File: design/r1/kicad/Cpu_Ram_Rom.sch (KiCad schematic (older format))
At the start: 14 parts, among them IC1 MC68010P10, U1 AT28C64B-15PU, U2 AT28C64B-15PU, U3 AS6C4008-55PCN, U4 AS6C4008-55PCN

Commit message: Initial cleanup
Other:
- note added: "1"
- note added: "CPU, RAM & ROM"
- note added: "Copyright ©2019-2020 Ross Bamford and Contributors.\nOpen Source Hardware licenced under CERN Open Hardware Licence. \nSee https://github.com/roscopeco/rosco_m68k/blob/master/LICENCE.hardware.txt\nOSHWA UK000006 (https://certification.oshwa.org/uk000006.html)\n"
- note removed: "CPU, RAM\n& ROM"
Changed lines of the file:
@@
-$EndComp
-$Comp
-L rosco_m68k-eagle-import:A3L-LOC #FRAME1
-U 1 1 CBB98AC2
-P 900 10700
-AR Path="/CBB98AC2" Ref="#FRAME1"  Part="1"
-AR Path="/5E53B4B8/CBB98AC2" Ref="#FRAME1"  Part="1"
-F 0 "#FRAME1" H 900 10700 50  0001 C CNN
-F 1 "CPU" H 900 10700 50  0001 C CNN
-F 2 "" H 900 10700 50  0001 C CNN
-F 3 "" H 900 10700 50  0001 C CNN
-	1    900  10700
-	1    0    0    -1
 $EndComp
 $Comp
@@
 Text Notes 14100 8900 0    59   ~ 0
 EVEN
-Text Notes 12700 10400 0    170  ~ 0
-CPU, RAM\n& ROM
 NoConn ~ 4400 2400
 NoConn ~ 4400 2500
@@
 Wire Bus Line
 	7500 550  7500 2600
+Connection ~ 7500 550
+Wire Bus Line
+	7500 550  2500 550
+Text Notes 19800 10900 0    50   ~ 0
+1
+Text Notes 16550 10750 0    79   ~ 0
+CPU, RAM & ROM
+Text Notes 16200 10200 0    59   ~ 0
+Copyright ©2019-2020 Ross Bamford and Contributors.\nOpen Source Hardware licenced under CERN Open Hardware Licence. \nSee https://github.com/roscopeco/rosco_m68k/blob/master/LICENCE.hardware.txt\nOSHWA UK000006 (https://certification.oshwa.org/uk000006.html)\n
 Wire Bus Line
 	11900 5300 11900 6100
@@
 Wire Bus Line
 	11450 2900 11450 4800
-Connection ~ 7500 550
-Wire Bus Line
-	7500 550  2500 550
 $EndSCHEMATC

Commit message: Cleanup first pass
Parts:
- U3, U4: symbol rosco_m68k-eagle-import:AS6C4008-55PCN -> rosco_m68k-rescue:AS6C4008-55PCN-rosco_m68k-eagle-import
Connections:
- net labels added: HALT, RAMOE, RW
- net labels removed: /HALT, /RAMOE, CONTROL:AS,BERR,BG,BGACK,BR,CLK,DTACK,EVENRAMSEL,EVENROMSEL,EXPSEL,FC0,FC1,FC2,IOSEL,IPL0,IPL1,IPL2,LDS,ODDRAMSEL,ODDROMSEL,RESET,R/W,UDS, R/W
- wire segments 240 -> 219
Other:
- moved on the sheet: C1, C2, C3, C4, C5, C6, C7, C8, IC1A, IC1B, R1, U1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

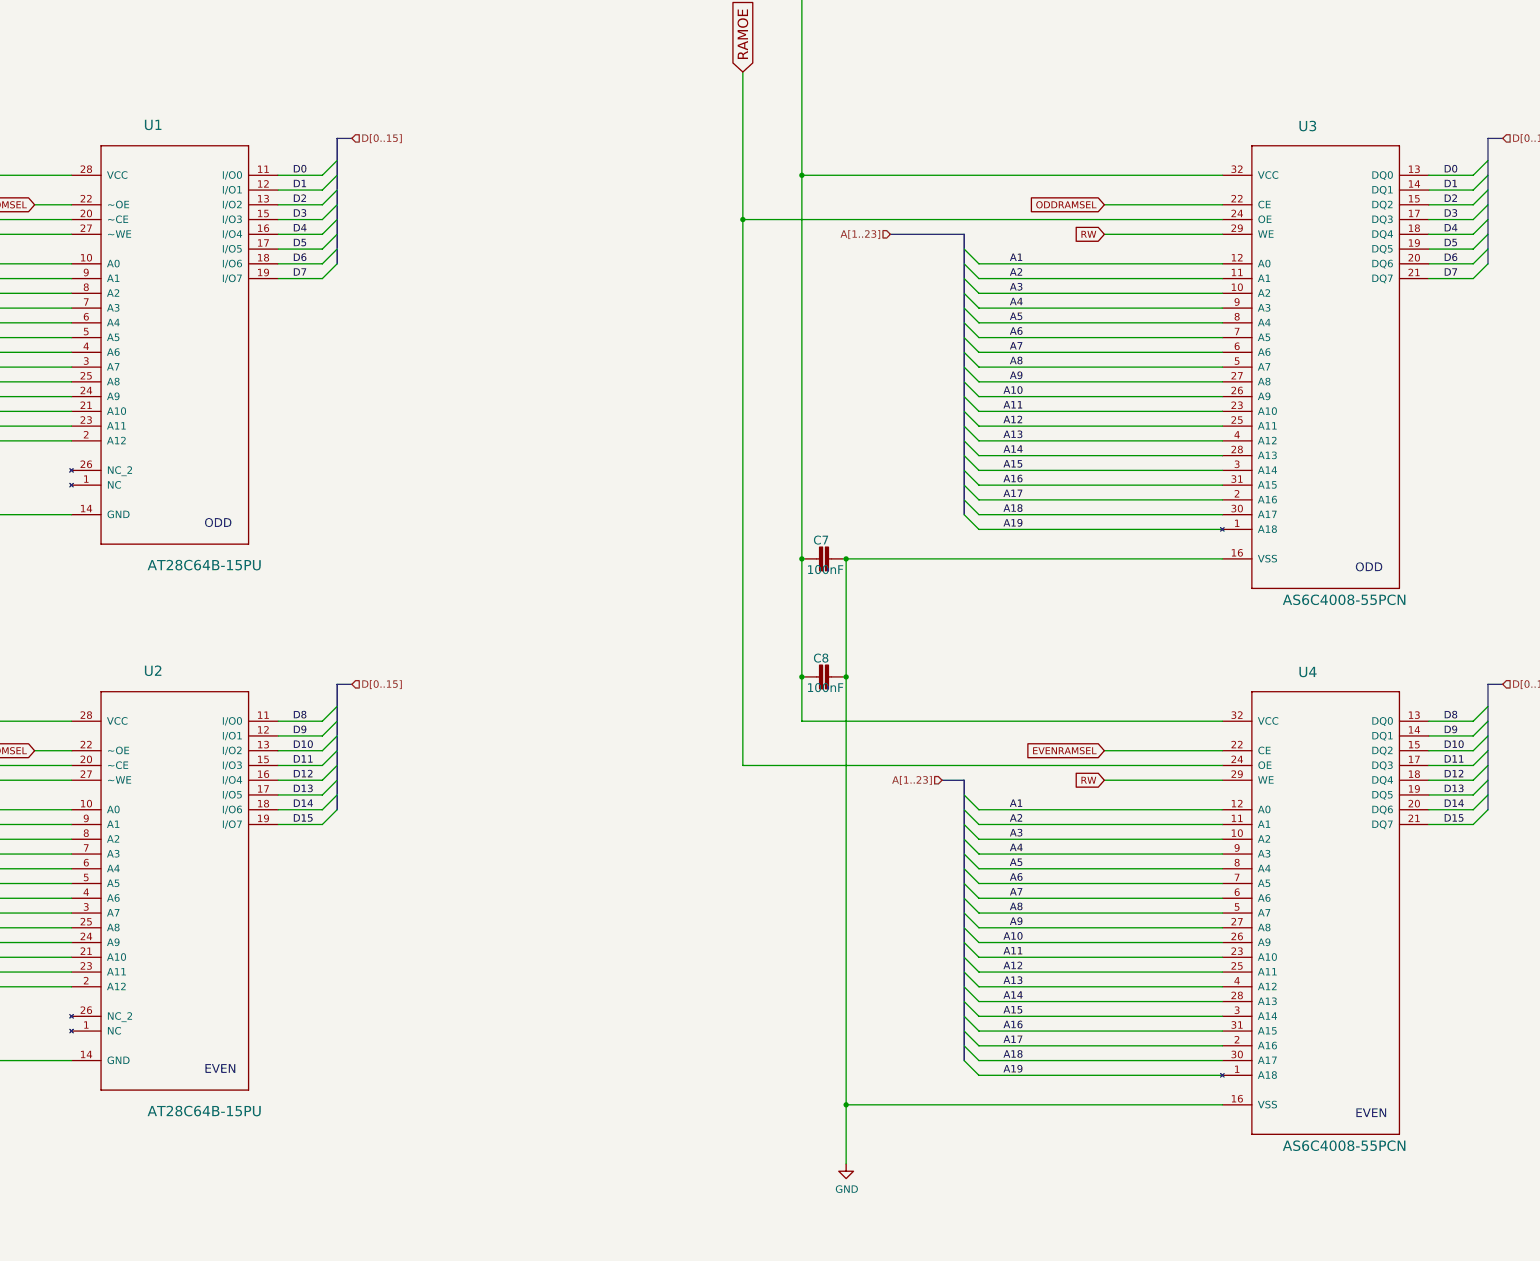
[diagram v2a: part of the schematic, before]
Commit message: Fixing migrated symbols
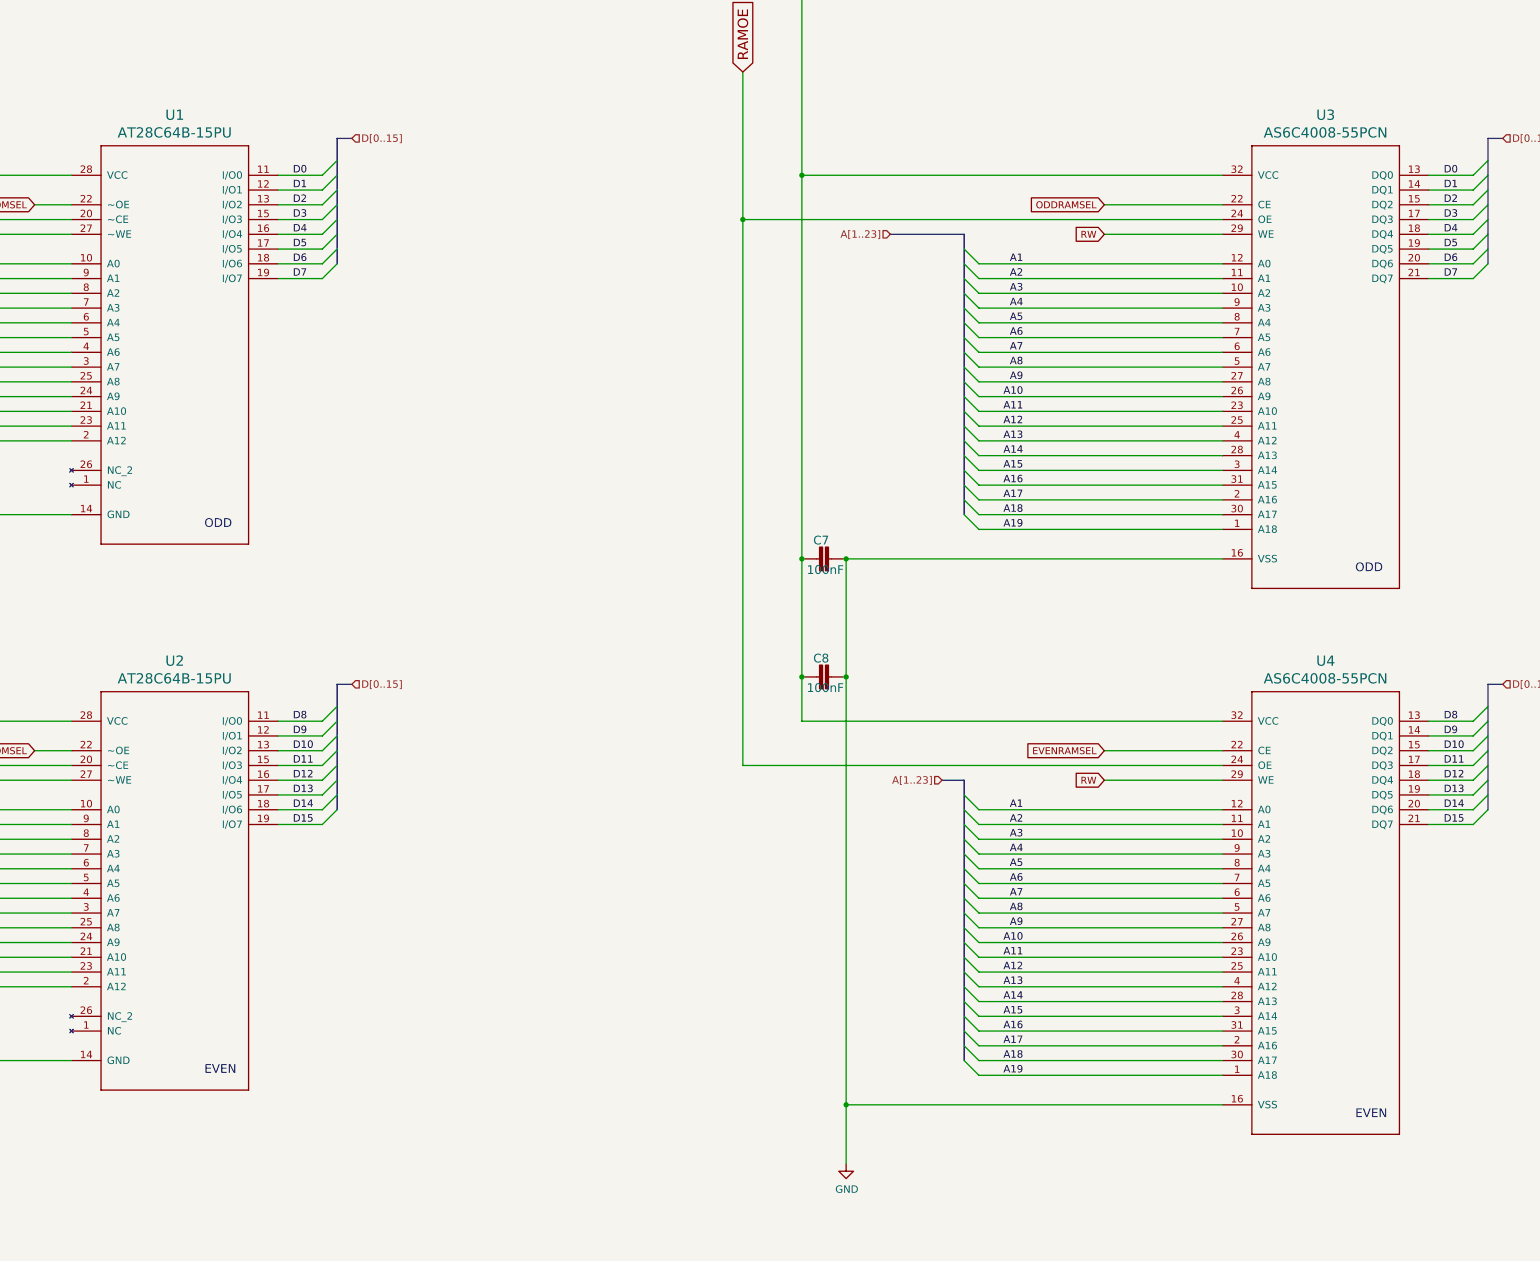
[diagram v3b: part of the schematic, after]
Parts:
- removed U3, U4: AS6C4008-55PCN, rosco_m68k:DIP254P1524X393-32, symbol rosco_m68k-rescue:AS6C4008-55PCN-rosco_m68k-eagle-import
- added U3, U4: AS6C4008-55PCN, symbol rosco_m68k-eagle-import:AS6C4008-55PCN
- U1, U2: footprint rosco_m68k:DIP254P1524X482-28 -> (none)
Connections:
- net A1: now also U3.12 (A0), U4.12 (A0)
- net A10: now also U3.26 (A9), U4.26 (A9)
- net A11: now also U3.23 (A10), U4.23 (A10)
- net A12: now also U3.25 (A11), U4.25 (A11)
- net A13: now also U3.4 (A12), U4.4 (A12)
- net A14: now also U3.28 (A13), U4.28 (A13)
- net A15: now also U3.3 (A14), U4.3 (A14)
- net A16: now also U3.31 (A15), U4.31 (A15)
- net A17: now also U3.2 (A16), U4.2 (A16)
- net A18: now also U3.30 (A17), U4.30 (A17)
- net A19: now also U3.1 (A18), U4.1 (A18)
- net A2: now also U3.11 (A1), U4.11 (A1)
- net A3: now also U3.10 (A2), U4.10 (A2)
- net A4: now also U3.9 (A3), U4.9 (A3)
- net A5: now also U3.8 (A4), U4.8 (A4)
- net A6: now also U3.7 (A5), U4.7 (A5)
- net A7: now also U3.6 (A6), U4.6 (A6)
- net A8: now also U3.5 (A7), U4.5 (A7)
- net A9: now also U3.27 (A8), U4.27 (A8)
- net D0: now also U3.13 (DQ0)
- net D1: now also U3.14 (DQ1)
- net D10: now also U4.15 (DQ2)
- net D11: now also U4.17 (DQ3)
- net D12: now also U4.18 (DQ4)
- net D13: now also U4.19 (DQ5)
- net D14: now also U4.20 (DQ6)
- net D15: now also U4.21 (DQ7)
- net D2: now also U3.15 (DQ2)
- net D3: now also U3.17 (DQ3)
- net D4: now also U3.18 (DQ4)
- net D5: now also U3.19 (DQ5)
- net D6: now also U3.20 (DQ6)
- net D7: now also U3.21 (DQ7)
- net D8: now also U4.13 (DQ0)
- net D9: now also U4.14 (DQ1)
- net EVENRAMSEL: now also U4.22 (CE)
- net GND: now also U3.16 (VSS), U4.16 (VSS)
- net ODDRAMSEL: now also U3.22 (CE)
- net RAMOE: now also U3.24 (OE), U4.24 (OE)
- net RW: now also U3.29 (WE), U4.29 (WE)
- net VCC: now also U3.32 (VCC), U4.32 (VCC)
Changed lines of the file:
@@
 	4400 5650 4500 5550
-$Comp
-L rosco_m68k-rescue:AS6C4008-55PCN-rosco_m68k-eagle-import U3
-U 1 1 9A04CEE8
-P 18250 3650
-AR Path="/9A04CEE8" Ref="U3"  Part="1"
-AR Path="/5E53B4B8/9A04CEE8" Ref="U3"  Part="1"
-F 0 "U3" H 18064 5141 69  0000 L BNN
-F 1 "AS6C4008-55PCN" H 17959 1930 69  0000 L BNN
-F 2 "rosco_m68k:DIP254P1524X393-32" H 18250 3650 50  0001 C CNN
-F 3 "" H 18250 3650 50  0001 C CNN
-	1    18250 3650
-	1    0    0    -1
-$EndComp
-$Comp
-L rosco_m68k-eagle-import:AT28C64B-15PU U1
-U 1 1 F9562130
-P 10450 3450
-AR Path="/F9562130" Ref="U1"  Part="1"
-AR Path="/5E53B4B8/F9562130" Ref="U1"  Part="1"
-F 0 "U1" H 10239 4749 69  0000 L BNN
-F 1 "AT28C64B-15PU" H 10265 1765 69  0000 L BNN
-F 2 "rosco_m68k:DIP254P1524X482-28" H 10450 3450 50  0001 C CNN
-F 3 "" H 10450 3450 50  0001 C CNN
-	1    10450 3450
-	1    0    0    -1
-$EndComp
-$Comp
-L rosco_m68k-eagle-import:AT28C64B-15PU U2
-U 1 1 C2DEB937
-P 10450 7150
-AR Path="/C2DEB937" Ref="U2"  Part="1"
-AR Path="/5E53B4B8/C2DEB937" Ref="U2"  Part="1"
-F 0 "U2" H 10239 8449 69  0000 L BNN
-F 1 "AT28C64B-15PU" H 10265 5465 69  0000 L BNN
-F 2 "rosco_m68k:DIP254P1524X482-28" H 10450 7150 50  0001 C CNN
-F 3 "" H 10450 7150 50  0001 C CNN
-	1    10450 7150
-	1    0    0    -1
-$EndComp
 $Comp
 L rosco_m68k-eagle-import:MC68000P IC1
@@
 NoConn ~ 3600 2850
 NoConn ~ 3600 2950
-$Comp
-L rosco_m68k-rescue:AS6C4008-55PCN-rosco_m68k-eagle-import U4
-U 1 1 7C57E89D
-P 18250 7350
-AR Path="/7C57E89D" Ref="U4"  Part="1"
-AR Path="/5E53B4B8/7C57E89D" Ref="U4"  Part="1"
-F 0 "U4" H 18064 8841 69  0000 L BNN
-F 1 "AS6C4008-55PCN" H 17959 5630 69  0000 L BNN
-F 2 "rosco_m68k:DIP254P1524X393-32" H 18250 7350 50  0001 C CNN
-F 3 "" H 18250 7350 50  0001 C CNN
-	1    18250 7350
-	1    0    0    -1
-$EndComp
 Text Label 2000 4550 0    50   ~ 0
 D0
@@
 Wire Wire Line
 	15900 8550 17550 8550
+$Comp
+L rosco_m68k-eagle-import:AS6C4008-55PCN U3
+U 1 1 5FE46869
+P 18250 3650
+F 0 "U3" H 18250 5258 69  0000 C CNN
+F 1 "AS6C4008-55PCN" H 18250 5138 69  0000 C CNN
+F 2 "" H 18250 3650 50  0001 C CNN
+F 3 "" H 18250 3650 50  0001 C CNN
+	1    18250 3650
+	1    0    0    -1
+$EndComp
+$Comp
+L rosco_m68k-eagle-import:AS6C4008-55PCN U4
+U 1 1 5FE4AB28
+P 18250 7350
+F 0 "U4" H 18250 8958 69  0000 C CNN
+F 1 "AS6C4008-55PCN" H 18250 8838 69  0000 C CNN
+F 2 "" H 18250 7350 50  0001 C CNN
+F 3 "" H 18250 7350 50  0001 C CNN
+	1    18250 7350
+	1    0    0    -1
+$EndComp
 Wire Bus Line
 	19350 5900 19350 6750
@@
 Wire Bus Line
 	15800 6550 15800 8450
+$Comp
+L rosco_m68k-eagle-import:AT28C64B-15PU U1
+U 1 1 5FF11175
+P 10450 3450
+F 0 "U1" H 10450 4858 69  0000 C CNN
+F 1 "AT28C64B-15PU" H 10450 4738 69  0000 C CNN
+F 2 "" H 10450 3450 50  0001 C CNN
+F 3 "" H 10450 3450 50  0001 C CNN
+	1    10450 3450
+	1    0    0    -1
+$EndComp
+$Comp
+L rosco_m68k-eagle-import:AT28C64B-15PU U2
+U 1 1 5FF13753
+P 10450 7150
+F 0 "U2" H 10450 8558 69  0000 C CNN
+F 1 "AT28C64B-15PU" H 10450 8438 69  0000 C CNN
+F 2 "" H 10450 7150 50  0001 C CNN
+F 3 "" H 10450 7150 50  0001 C CNN
+	1    10450 7150
+	1    0    0    -1
+$EndComp
 $EndSCHEMATC

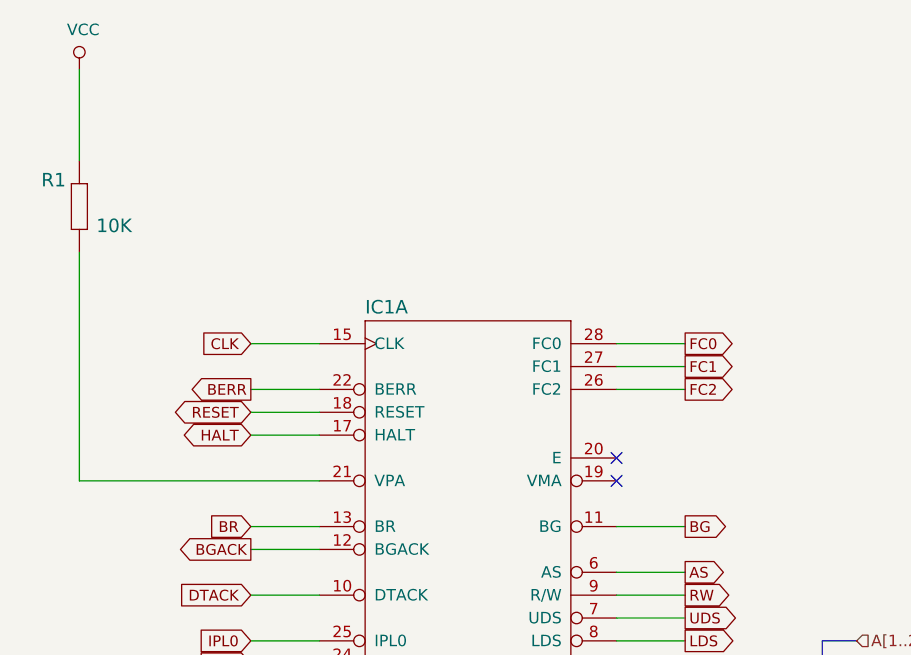
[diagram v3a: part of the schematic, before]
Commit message: GPIO, Legacy Peripheral and Panel support
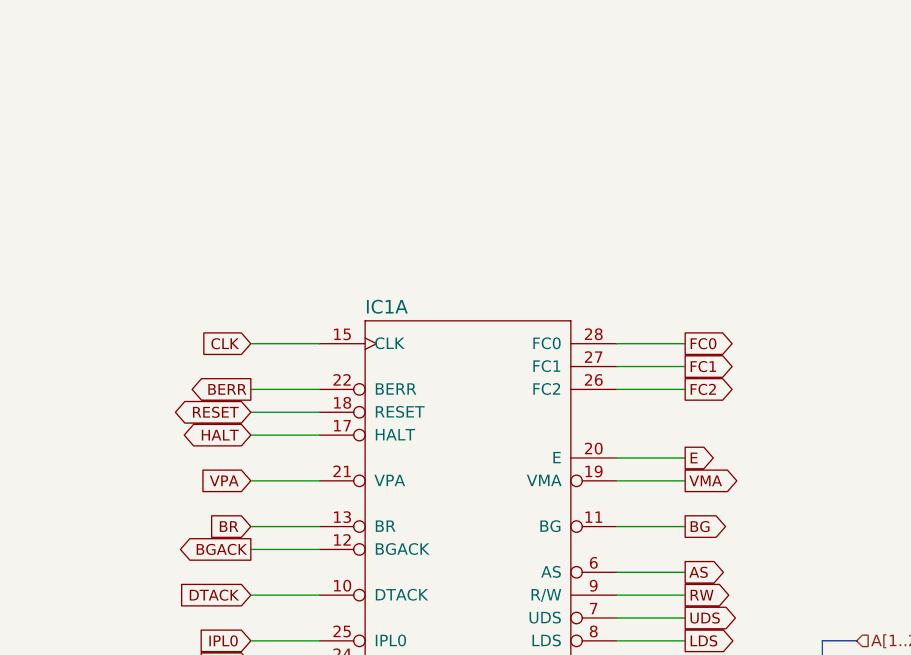
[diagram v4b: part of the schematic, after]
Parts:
- removed R1: 10K, rosco_m68k:0207_10, symbol rosco_m68k-eagle-import:R-EU_0207_10
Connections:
- net VPA: now reaches IC1.21 (VPA)
- net VMA: now reaches IC1.19 (VMA)
- net E: now reaches IC1.20 (E)
- no-connect marks 2 -> 0
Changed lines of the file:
@@
 Text Notes 18450 8850 0    59   ~ 0
 EVEN
-NoConn ~ 3600 2850
-NoConn ~ 3600 2950
 Text Label 2000 4550 0    50   ~ 0
 D0
@@
 	1    0    0    -1
 $EndComp
-$Comp
-L power:VCC #PWR0105
-U 1 1 5EAC6AC0
-P 1250 1150
-F 0 "#PWR0105" H 1250 1000 50  0001 C CNN
-F 1 "VCC" H 1267 1323 50  0000 C CNN
-F 2 "" H 1250 1150 50  0001 C CNN
-F 3 "" H 1250 1150 50  0001 C CNN
-	1    1250 1150
-	1    0    0    -1
-$EndComp
 Wire Wire Line
 	7900 2450 7900 1150
@@
 	8200 4750 8200 2750
 Wire Wire Line
-	1250 2950 2300 2950
-Wire Wire Line
-	1250 1150 1250 1550
-Wire Wire Line
-	1250 1950 1250 2950
-$Comp
-L rosco_m68k-eagle-import:R-EU_0207_10 R1
-U 1 1 4C88E097
-P 1250 1750
-AR Path="/4C88E097" Ref="R1"  Part="1"
-AR Path="/5E53B4B8/4C88E097" Ref="R1"  Part="1"
-F 0 "R1" V 1400 1809 59  0000 L BNN
-F 1 "10K" V 1200 1520 59  0000 L BNN
-F 2 "rosco_m68k:0207_10" H 1250 1750 50  0001 C CNN
-F 3 "" H 1250 1750 50  0001 C CNN
-	1    1250 1750
-	0    -1   -1   0
-$EndComp
-Wire Wire Line
 	2000 2750 2300 2750
 Wire Wire Line
@@
 	1    0    0    -1
 $EndComp
-Wire Bus Line
-	19350 5900 19350 6750
-Wire Bus Line
-	19350 2200 19350 3050
-Wire Bus Line
-	11550 5900 11550 6750
-Wire Bus Line
-	11550 2200 11550 3050
-Wire Bus Line
-	8850 5900 8850 7850
-Wire Bus Line
-	8850 2250 8850 4150
-Wire Bus Line
-	1600 4300 1600 5950
-Wire Bus Line
-	15800 2850 15800 4750
-Wire Bus Line
-	4500 3650 4500 5950
-Wire Bus Line
-	15800 6550 15800 8450
 $Comp
 L rosco_m68k-eagle-import:AT28C64B-15PU U1
@@
 	1    0    0    -1
 $EndComp
+Wire Wire Line
+	3600 2850 3900 2850
+Wire Wire Line
+	3600 2950 3900 2950
+Wire Wire Line
+	2300 2950 2000 2950
+Text GLabel 2000 2950 0    47   Input ~ 0
+VPA
+Text GLabel 3900 2950 2    47   Output ~ 0
+VMA
+Text GLabel 3900 2850 2    47   Output ~ 0
+E
+Wire Bus Line
+	19350 5900 19350 6750
+Wire Bus Line
+	19350 2200 19350 3050
+Wire Bus Line
+	11550 5900 11550 6750
+Wire Bus Line
+	11550 2200 11550 3050
+Wire Bus Line
+	8850 5900 8850 7850
+Wire Bus Line
+	8850 2250 8850 4150
+Wire Bus Line
+	1600 4300 1600 5950
+Wire Bus Line
+	15800 2850 15800 4750
+Wire Bus Line
+	4500 3650 4500 5950
+Wire Bus Line
+	15800 6550 15800 8450
 $EndSCHEMATC
